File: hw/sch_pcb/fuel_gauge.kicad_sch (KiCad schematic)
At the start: 36 parts, among them J10 HEADER_2x01_PARALLEL, J11 HEADER_1x02, Q2 AP2305AGN-HF-3, Q3 DMT31M7LPS, Q5 DMT31M7LPS, SW1 SW_Push, SW2 SW_Push, U3 BQ40z50-R2

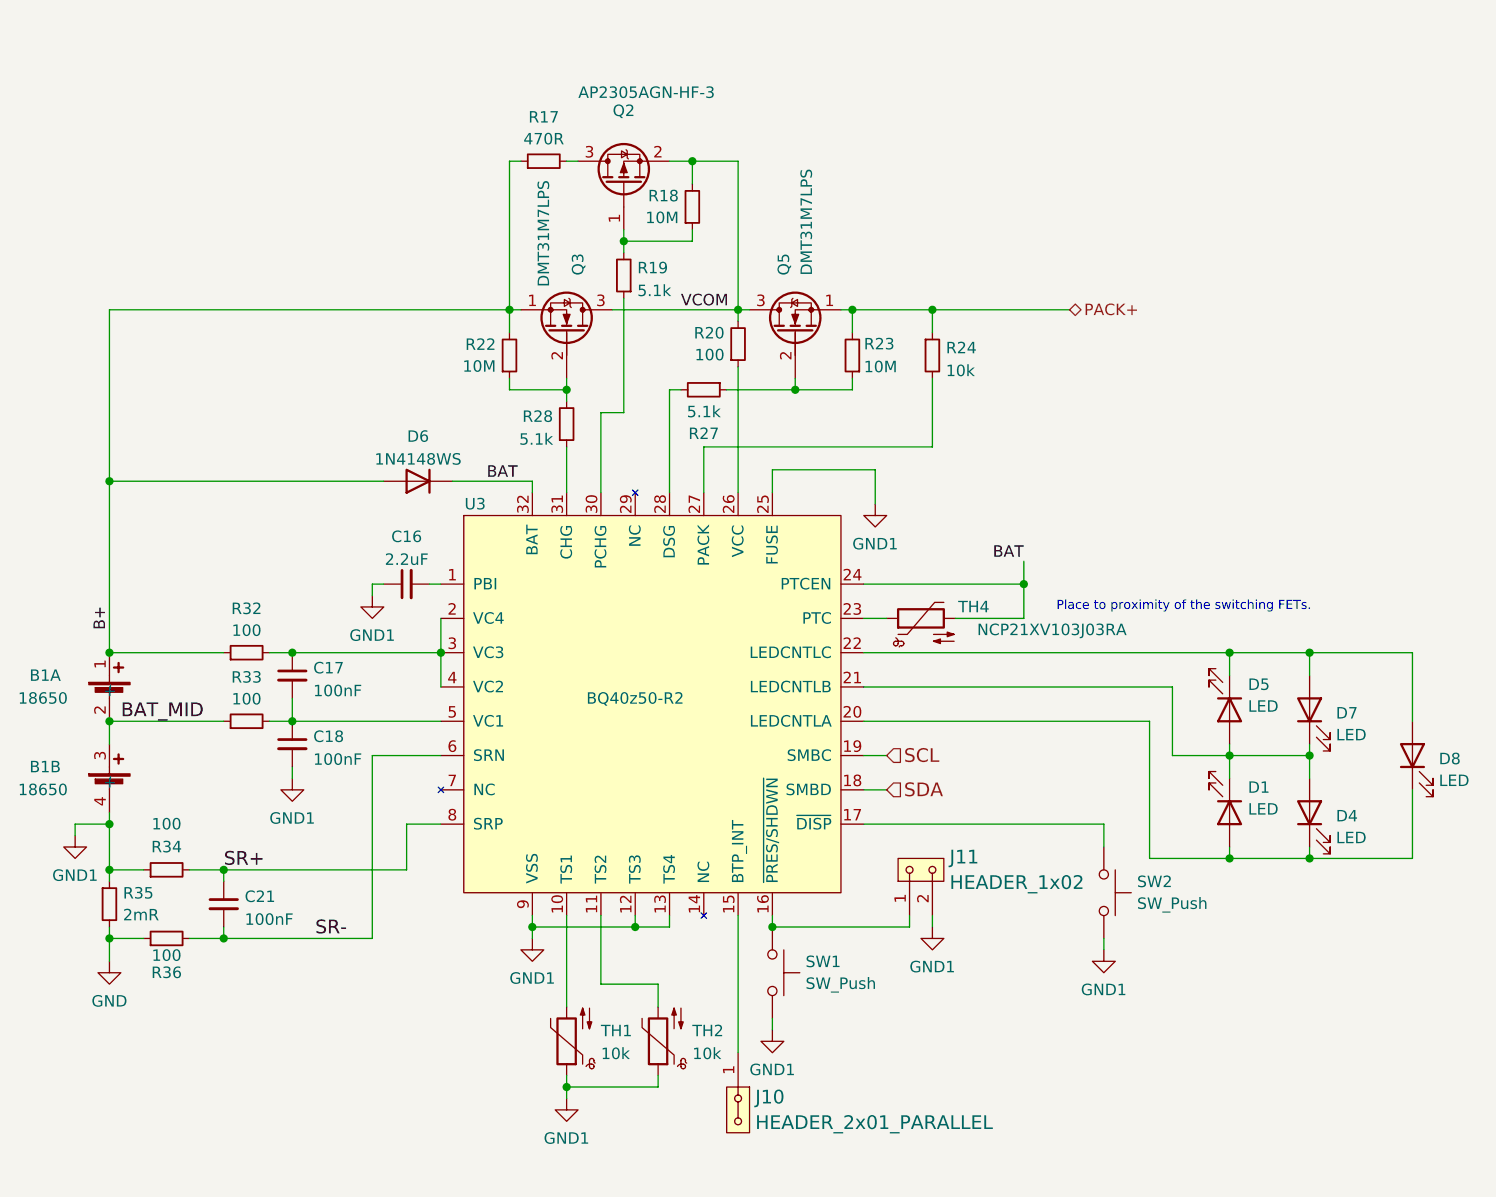
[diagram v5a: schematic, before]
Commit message: USB data lines layout improvement. Zones definitions for improving noise imunity.
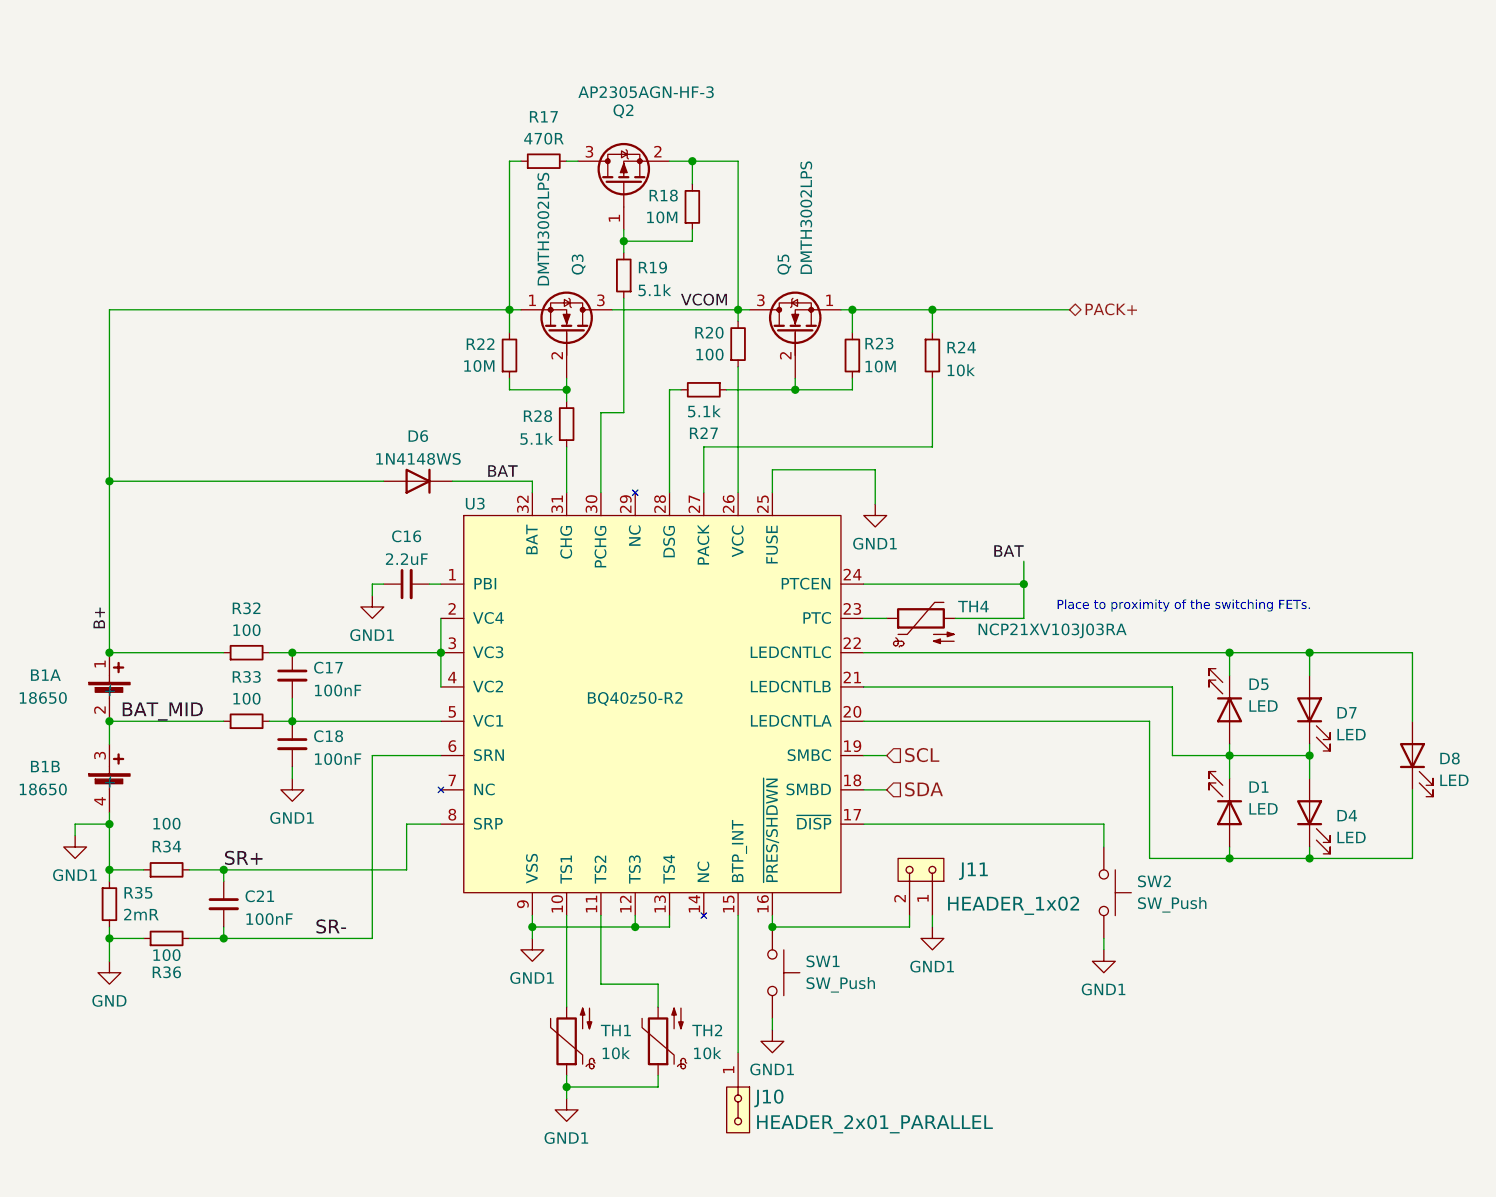
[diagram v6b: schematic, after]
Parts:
- J10, J11: footprint Mlab_Pin_Headers:Straight_1x02 -> Mlab_Pin_Headers:Straight_2x01
- Q3, Q5: value DMT31M7LPS -> DMTH3002LPS
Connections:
- net GND1: now also J11.1; no longer J11.2
- net at SW1.1, U3.16 (~{PRES/SHDWN}): now also J11.2; no longer J11.1
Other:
- moved on the sheet: J11
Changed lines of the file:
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@@
 			)
 		)
-		(property "Value" "DMT31M7LPS"
+		(property "Value" "DMTH3002LPS"
 			(at 110.49 63.5 0)
 			(effects
@@
 			)
 		)
-		(property "Datasheet" "https://eu.mouser.com/datasheet/2/115/DIOD_S_A0006645066_1-2542967.pdf"
+		(property "Datasheet" "https://eu.mouser.com/datasheet/2/115/DIOD_S_A0003132884_1-2542222.pdf"
 			(at 113.03 68.58 0)
 			(effects
@@
 	(symbol
 		(lib_id "MLAB_HEADER:HEADER_1x02")
-		(at 152.4 128.27 90)
-		(unit 1)
-		(exclude_from_sim no)
-		(in_bom yes)
-		(on_board yes)
-		(dnp no)
-		(fields_autoplaced yes)
+		(at 152.4 128.27 270)
+		(mirror x)
+		(unit 1)
+		(exclude_from_sim no)
+		(in_bom yes)
+		(on_board yes)
+		(dnp no)
 		(property "Reference" "J11"
-			(at 155.575 126.8535 90)
+			(at 160.02 128.27 90)
 			(effects
 				(font
@@
 		)
 		(property "Value" "HEADER_1x02"
-			(at 155.575 129.6864 90)
+			(at 170.18 132.08 90)
 			(effects
 				(font
@@
 			)
 		)
-		(property "Footprint" "Mlab_Pin_Headers:Straight_1x02"
-			(at 151.13 128.27 0)
+		(property "Footprint" "Mlab_Pin_Headers:Straight_2x01"
+			(at 153.67 128.27 0)
 			(effects
 				(font
@@
 		)
 		(property "Datasheet" ""
-			(at 151.13 128.27 0)
+			(at 153.67 128.27 0)
 			(effects
 				(font
@@
 			)
 		)
-		(property "Value" "DMT31M7LPS"
+		(property "Value" "DMTH3002LPS"
 			(at 139.7 62.23 0)
 			(effects
@@
 			)
 		)
-		(property "Datasheet" "https://eu.mouser.com/datasheet/2/115/DIOD_S_A0006645066_1-2542967.pdf"
+		(property "Datasheet" "https://eu.mouser.com/datasheet/2/115/DIOD_S_A0003132884_1-2542222.pdf"
 			(at 138.43 68.58 0)
 			(effects
@@
 			)
 		)
-		(property "Footprint" "Mlab_Pin_Headers:Straight_1x02"
+		(property "Footprint" "Mlab_Pin_Headers:Straight_2x01"
 			(at 132.08 154.94 0)
 			(effects

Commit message: Update USTids.
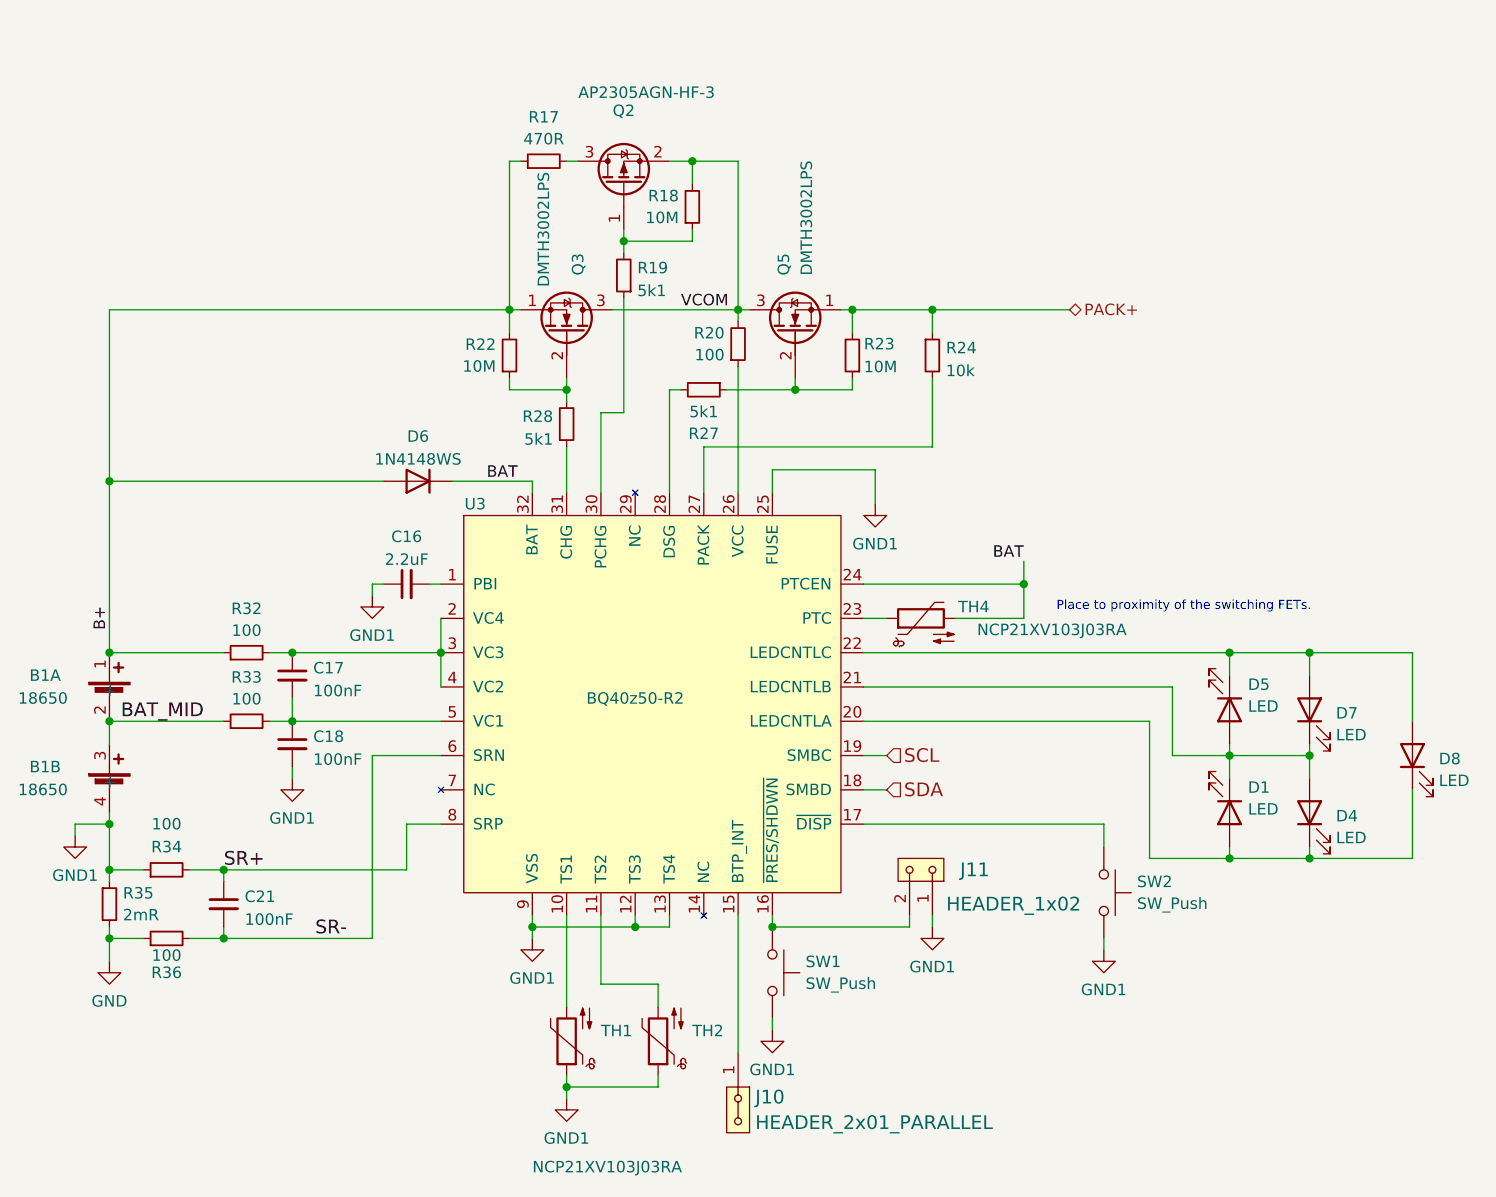
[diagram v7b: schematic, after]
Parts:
- C16: LCSC C23630 -> (none); UST_ID (none) -> 5c70984712875079b91f8b51
- C17, C18, C21: UST_ID (none) -> 5c70984712875079b91f8b4c
- D1, D4, D5, D7, D8: UST_ID (none) -> 5c70984412875079b91f8892
- R17: LCSC C17887 -> (none); UST_ID (none) -> 60be2ed51287500165e6c1cd
- R18, R22, R23: UST_ID (none) -> 5c70984712875079b91f8aae
- R19, R27, R28: value 5.1k -> 5k1; UST_ID (none) -> 5fa0fc3e12875025b3977997
- R20, R32, R33, R34, R36: UST_ID (none) -> 5c70984512875079b91f8977
- R24: UST_ID (none) -> 5c70984612875079b91f899f
- SW1, SW2: UST_ID (none) -> 5c70984712875079b91f8ad2
- TH1, TH2: value 10k -> NCP21XV103J03RA; UST_ID (none) -> 5c70984712875079b91f8ac5
- U3: UST_ID (none) -> 66a15dd06fdfe6f54e2ebf93
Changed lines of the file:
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@@
 			)
 		)
+		(property "UST_ID" "5c70984612875079b91f899f"
+			(at 153.67 71.12 0)
+			(effects
+				(font
+					(size 1.27 1.27)
+				)
+				(hide yes)
+			)
+		)
 		(pin "1"
 		)
@@
 			)
 		)
+		(property "UST_ID" "5c70984512875079b91f8977"
+			(at 77.47 111.76 0)
+			(effects
+				(font
+					(size 1.27 1.27)
+				)
+				(hide yes)
+			)
+		)
 		(pin "1"
 		)
@@
 			)
 		)
+		(property "UST_ID" " 5c70984712875079b91f8b4c "
+			(at 74.93 132.08 0)
+			(effects
+				(font
+					(size 1.27 1.27)
+				)
+				(hide yes)
+			)
+		)
 		(pin "1"
 		)
@@
 			)
 		)
+		(property "UST_ID" "5c70984512875079b91f8977"
+			(at 68.58 128.27 0)
+			(effects
+				(font
+					(size 1.27 1.27)
+				)
+				(hide yes)
+			)
+		)
 		(pin "1"
 		)
@@
 			)
 		)
-		(property "Value" "5.1k"
+		(property "Value" "5k1"
 			(at 111.5315 80.4422 0)
 			(effects
@@
 			)
 		)
+		(property "UST_ID" "5fa0fc3e12875025b3977997 "
+			(at 113.03 78.74 0)
+			(effects
+				(font
+					(size 1.27 1.27)
+				)
+				(hide yes)
+			)
+		)
 		(pin "1"
 		)
@@
 			)
 		)
+		(property "UST_ID" "66a15dd06fdfe6f54e2ebf93"
+			(at 120.65 109.22 0)
+			(effects
+				(font
+					(size 1.27 1.27)
+				)
+				(hide yes)
+			)
+		)
 		(pin "1"
 		)
@@
 			)
 		)
+		(property "UST_ID" "5c70984412875079b91f8892"
+			(at 207.01 115.57 0)
+			(effects
+				(font
+					(size 1.27 1.27)
+				)
+				(hide yes)
+			)
+		)
 		(pin "1"
 		)
@@
 			)
 		)
-		(property "UST_ID" ""
+		(property "UST_ID" "5c70984712875079b91f8ad2"
 			(at 135.89 139.7 0)
 			(effects
@@
 			)
 		)
+		(property "UST_ID" "5c70984712875079b91f8aae"
+			(at 106.68 71.12 0)
+			(effects
+				(font
+					(size 1.27 1.27)
+				)
+				(hide yes)
+			)
+		)
 		(pin "1"
 		)
@@
 			)
 		)
-		(property "LCSC" "C23630"
-			(at 95.25 96.52 90)
+		(property "UST_ID" "5c70984712875079b91f8b51"
+			(at 95.25 96.52 0)
 			(effects
 				(font
@@
 			)
 		)
+		(property "UST_ID" " 5c70984712875079b91f8b4c "
+			(at 82.55 114.3 0)
+			(effects
+				(font
+					(size 1.27 1.27)
+				)
+				(hide yes)
+			)
+		)
 		(pin "1"
 		)
@@
 			)
 		)
+		(property "UST_ID" "5c70984712875079b91f8ad2"
+			(at 172.72 130.81 0)
+			(effects
+				(font
+					(size 1.27 1.27)
+				)
+				(hide yes)
+			)
+		)
 		(pin "2"
 		)
@@
 			)
 		)
+		(property "UST_ID" "5c70984412875079b91f8892"
+			(at 195.58 121.92 0)
+			(effects
+				(font
+					(size 1.27 1.27)
+				)
+				(hide yes)
+			)
+		)
 		(pin "1"
 		)
@@
 		(on_board yes)
 		(dnp no)
-		(fields_autoplaced yes)
 		(property "Reference" "TH2"
 			(at 127 146.1678 0)
@@
 			)
 		)
-		(property "Value" "10k"
-			(at 127 148.7047 0)
+		(property "Value" "NCP21XV103J03RA"
+			(at 124.46 170.18 90)
 			(effects
 				(font
@@
 				)
 				(justify right)
+				(hide yes)
 			)
 		)
@@
 			)
 		)
-		(property "UST_ID" ""
+		(property "UST_ID" "5c70984712875079b91f8ac5"
 			(at 123.19 147.32 0)
 			(effects
@@
 			)
 		)
-		(property "LCSC" "C17887"
-			(at 110.49 49.53 90)
+		(property "UST_ID" "60be2ed51287500165e6c1cd"
+			(at 110.49 49.53 0)
 			(effects
 				(font
@@
 			)
 		)
+		(property "UST_ID" "5c70984512875079b91f8977"
+			(at 77.47 104.14 0)
+			(effects
+				(font
+					(size 1.27 1.27)
+				)
+				(hide yes)
+			)
+		)
 		(pin "1"
 		)
@@
 			)
 		)
+		(property "UST_ID" "5c70984512875079b91f8977"
+			(at 132.08 69.85 0)
+			(effects
+				(font
+					(size 1.27 1.27)
+				)
+				(hide yes)
+			)
+		)
 		(pin "1"
 		)
@@
 			)
 		)
+		(property "UST_ID" "5c70984512875079b91f8977"
+			(at 68.58 135.89 0)
+			(effects
+				(font
+					(size 1.27 1.27)
+				)
+				(hide yes)
+			)
+		)
 		(pin "1"
 		)
@@
 			)
 		)
-		(property "Value" "5.1k"
+		(property "Value" "5k1"
 			(at 120.8786 63.9322 0)
 			(effects
@@
 			)
 		)
+		(property "UST_ID" "5fa0fc3e12875025b3977997 "
+			(at 119.38 62.23 0)
+			(effects
+				(font
+					(size 1.27 1.27)
+				)
+				(hide yes)
+			)
+		)
 		(pin "1"
 		)
@@
 			)
 		)
+		(property "UST_ID" "5c70984412875079b91f8892"
+			(at 186.69 121.92 0)
+			(effects
+				(font
+					(size 1.27 1.27)
+				)
+				(hide yes)
+			)
+		)
 		(pin "1"
 		)
@@
 			)
 		)
+		(property "UST_ID" "5c70984712875079b91f8aae"
+			(at 127 54.61 0)
+			(effects
+				(font
+					(size 1.27 1.27)
+				)
+				(hide yes)
+			)
+		)
 		(pin "1"
 		)
@@
 			)
 		)
+		(property "UST_ID" "5c70984412875079b91f8892"
+			(at 186.69 110.49 0)
+			(effects
+				(font
+					(size 1.27 1.27)
+				)
+				(hide yes)
+			)
+		)
 		(pin "1"
 		)
@@
 		(on_board yes)
 		(dnp no)
-		(fields_autoplaced yes)
 		(property "Reference" "TH1"
 			(at 116.84 146.1678 0)
@@
 			)
 		)
-		(property "Value" "10k"
-			(at 116.84 148.7047 0)
+		(property "Value" "NCP21XV103J03RA"
+			(at 109.22 161.29 0)
 			(effects
 				(font
@@
 			)
 		)
+		(property "UST_ID" "5c70984712875079b91f8ac5"
+			(at 113.03 147.32 0)
+			(effects
+				(font
+					(size 1.27 1.27)
+				)
+				(hide yes)
+			)
+		)
 		(pin "1"
 		)
@@
 			)
 		)
+		(property "UST_ID" "5c70984712875079b91f8aae"
+			(at 144.78 71.12 0)
+			(effects
+				(font
+					(size 1.27 1.27)
+				)
+				(hide yes)
+			)
+		)
 		(pin "1"
 		)
@@
 			)
 		)
+		(property "UST_ID" "5c70984412875079b91f8892"
+			(at 195.58 110.49 0)
+			(effects
+				(font
+					(size 1.27 1.27)
+				)
+				(hide yes)
+			)
+		)
 		(pin "1"
 		)
@@
 			)
 		)
+		(property "UST_ID" " 5c70984712875079b91f8b4c "
+			(at 82.55 106.68 0)
+			(effects
+				(font
+					(size 1.27 1.27)
+				)
+				(hide yes)
+			)
+		)
 		(pin "1"
 		)
@@
 			)
 		)
-		(property "Value" "5.1k"
+		(property "Value" "5k1"
 			(at 128.27 77.3867 90)
 			(effects
@@
 			(at 128.27 74.93 0)
 			(effects
+				(font
+					(size 1.27 1.27)
+				)
+				(hide yes)
+			)
+		)
+		(property "UST_ID" "5fa0fc3e12875025b3977997 "
+			(at 128.27 74.93 0)
+			(effects

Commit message: Fix missing assigments.
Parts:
- R19, R27, R28: UST_ID 5fa0fc3e12875025b3977997 -> 5fa0fc3e12875025b3977997
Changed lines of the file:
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@@
 			)
 		)
-		(property "UST_ID" "5fa0fc3e12875025b3977997 "
+		(property "UST_ID" "5fa0fc3e12875025b3977997"
 			(at 113.03 78.74 0)
 			(effects
@@
 			)
 		)
-		(property "UST_ID" "5fa0fc3e12875025b3977997 "
+		(property "UST_ID" "5fa0fc3e12875025b3977997"
 			(at 119.38 62.23 0)
 			(effects
@@
 			)
 		)
-		(property "UST_ID" "5fa0fc3e12875025b3977997 "
+		(property "UST_ID" "5fa0fc3e12875025b3977997"
 			(at 128.27 74.93 0)
 			(effects
